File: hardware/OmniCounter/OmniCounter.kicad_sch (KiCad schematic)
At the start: 1 part

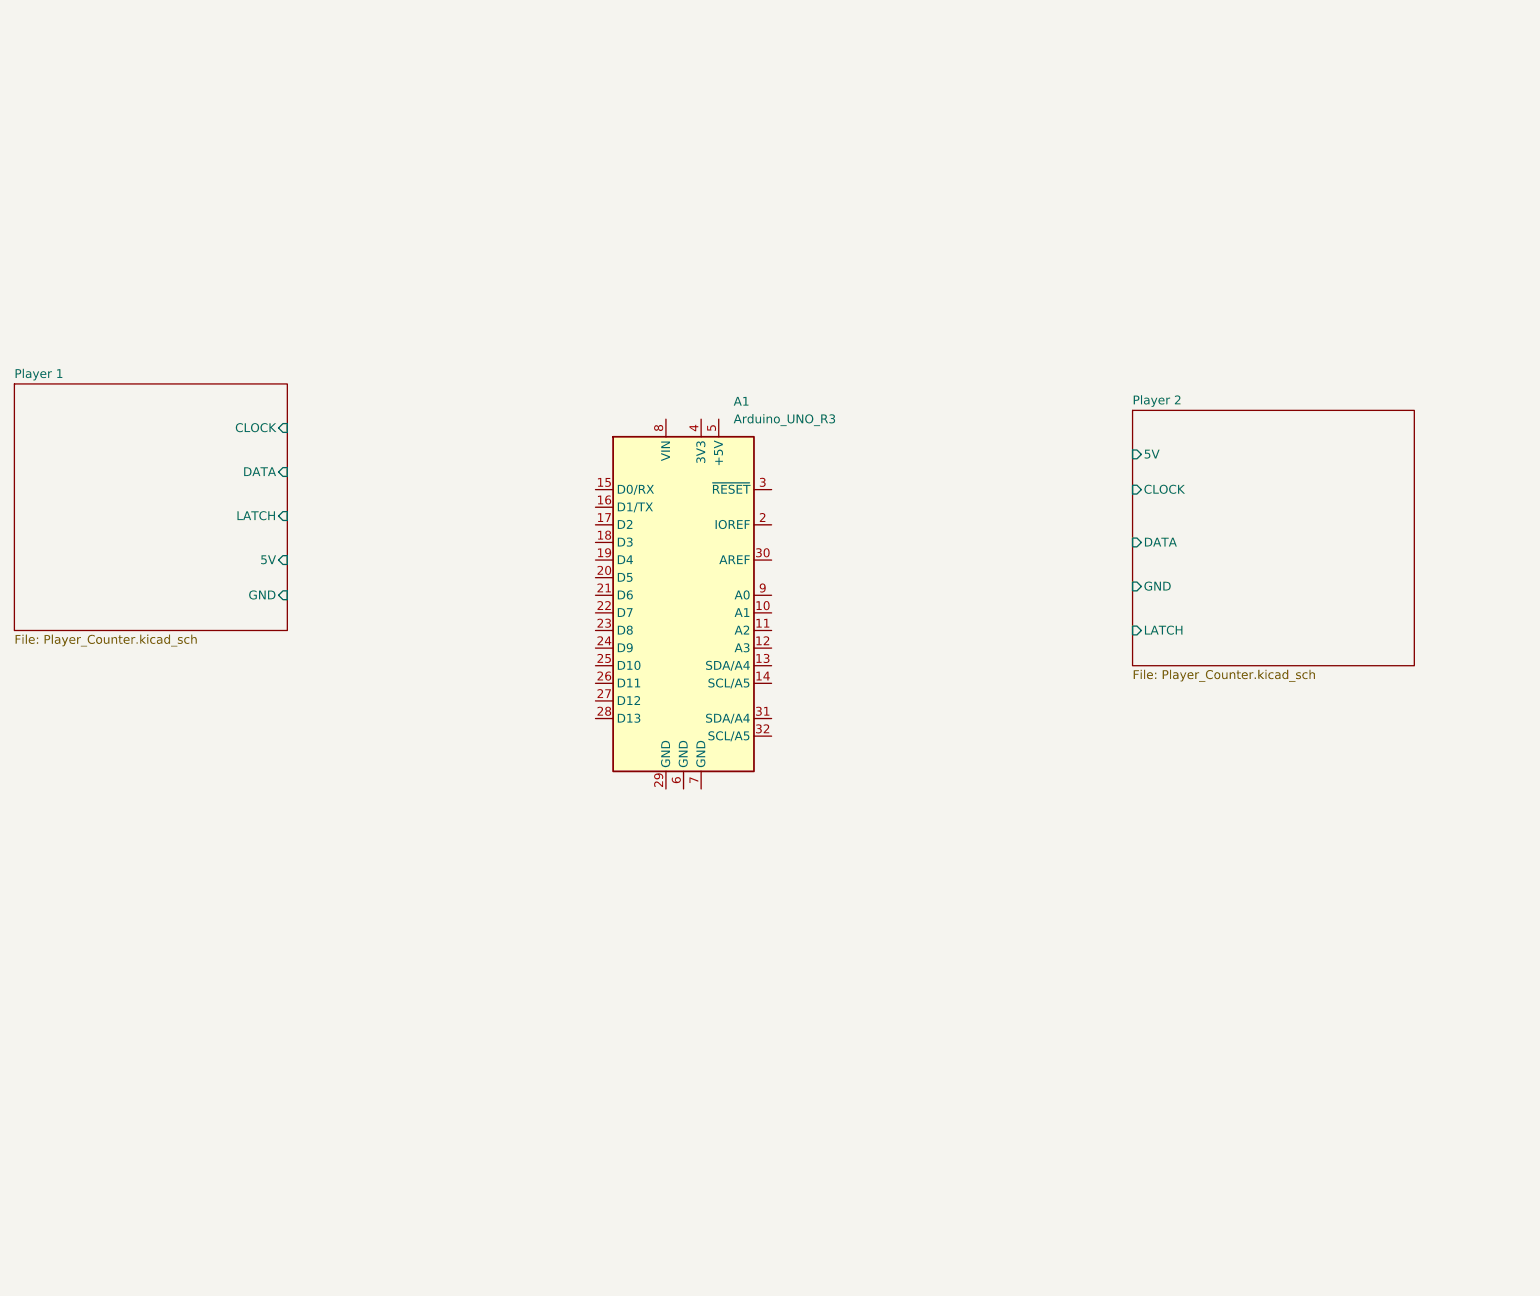
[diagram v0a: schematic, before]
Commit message: wired up rest of the tactile switches
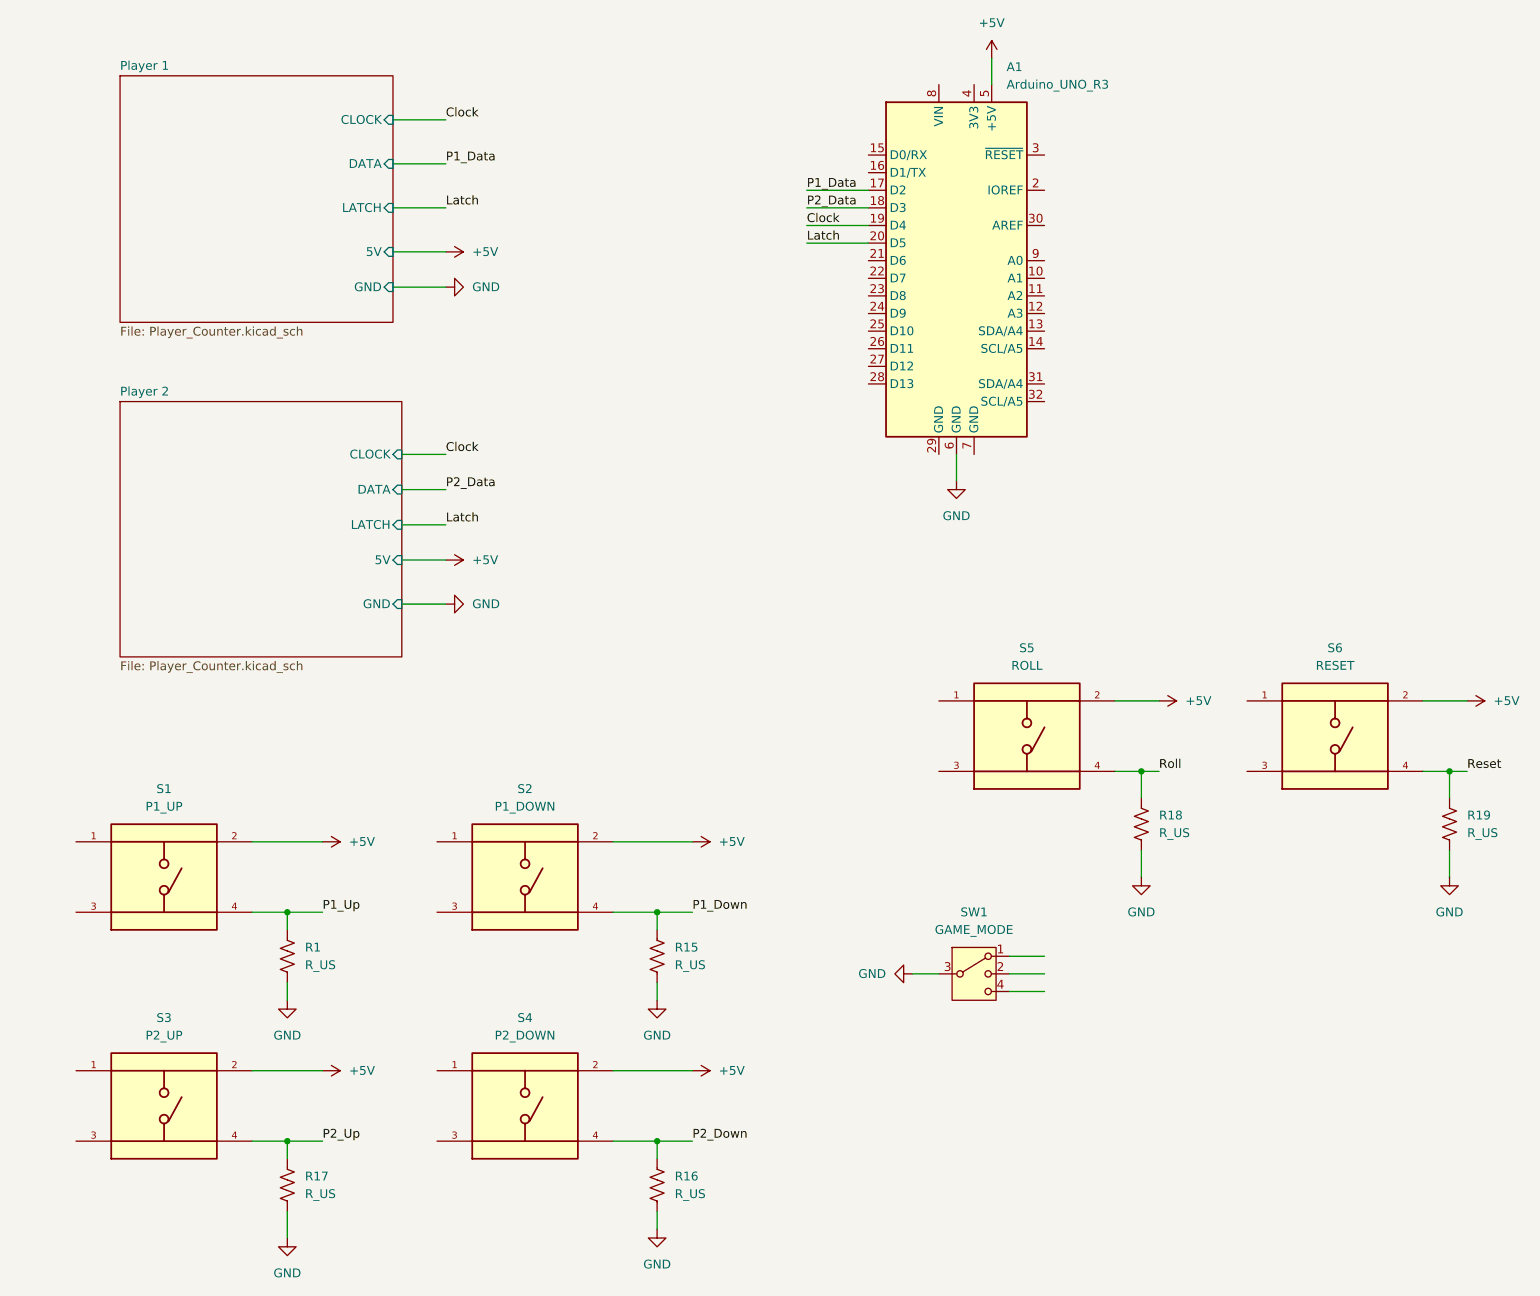
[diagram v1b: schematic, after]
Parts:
- added R1, R15, R16, R17, R18, R19: R_US, symbol Device:R_US
- added S1: P1_UP, TS02-66-60-BK-160-LCR-D:SW_TS02-66-60-BK-160-LCR-D, symbol TS02-66-60-BK-160-LCR-D:TS02-66-60-BK-160-LCR-D
- added S2: P1_DOWN, TS02-66-60-BK-160-LCR-D:SW_TS02-66-60-BK-160-LCR-D, symbol TS02-66-60-BK-160-LCR-D:TS02-66-60-BK-160-LCR-D
- added S3: P2_UP, TS02-66-60-BK-160-LCR-D:SW_TS02-66-60-BK-160-LCR-D, symbol TS02-66-60-BK-160-LCR-D:TS02-66-60-BK-160-LCR-D
- added S4: P2_DOWN, TS02-66-60-BK-160-LCR-D:SW_TS02-66-60-BK-160-LCR-D, symbol TS02-66-60-BK-160-LCR-D:TS02-66-60-BK-160-LCR-D
- added S5: ROLL, TS02-66-60-BK-160-LCR-D:SW_TS02-66-60-BK-160-LCR-D, symbol TS02-66-60-BK-160-LCR-D:TS02-66-60-BK-160-LCR-D
- added S6: RESET, TS02-66-60-BK-160-LCR-D:SW_TS02-66-60-BK-160-LCR-D, symbol TS02-66-60-BK-160-LCR-D:TS02-66-60-BK-160-LCR-D
- added SW1: GAME_MODE, symbol Switch:SW_SP3T
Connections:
- net P1_Data: now reaches A1.17 (D2)
- net P2_Data: now reaches A1.18 (D3)
- net Clock: now reaches A1.19 (D4)
- net Latch: now reaches A1.20 (D5)
- net +5V: now reaches A1.5 (+5V)
- net +5V: now also S1.2, S2.2, S3.2, S4.2, S5.2, S6.2
- net GND: now reaches A1.6 (GND)
- net GND: now also R1.2, R15.2, R16.2, R17.2, R18.2, R19.2, SW1.3
- new net: R1.1, S1.4
- new net P1_Down: R15.1, S2.4
- new net P2_Down: R16.1, S4.4
- new net P2_Up: R17.1, S3.4
- new net Reset: R19.1, S6.4
- new net Roll: R18.1, S5.4
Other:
- moved on the sheet: A1
